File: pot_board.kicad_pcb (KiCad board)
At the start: 2 copper layers, 190.5 x 45.7 mm, 40 parts, among them J1 Power, J2 Conn 1x3, J3 Conn 1x3, J4 Conn 1x3, J5 Conn 1x3, J6 Conn 1x3, J7 Conn 1x3, J8 Conn 1x3, J9 Conn 1x3, SW1 SW_SPDT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

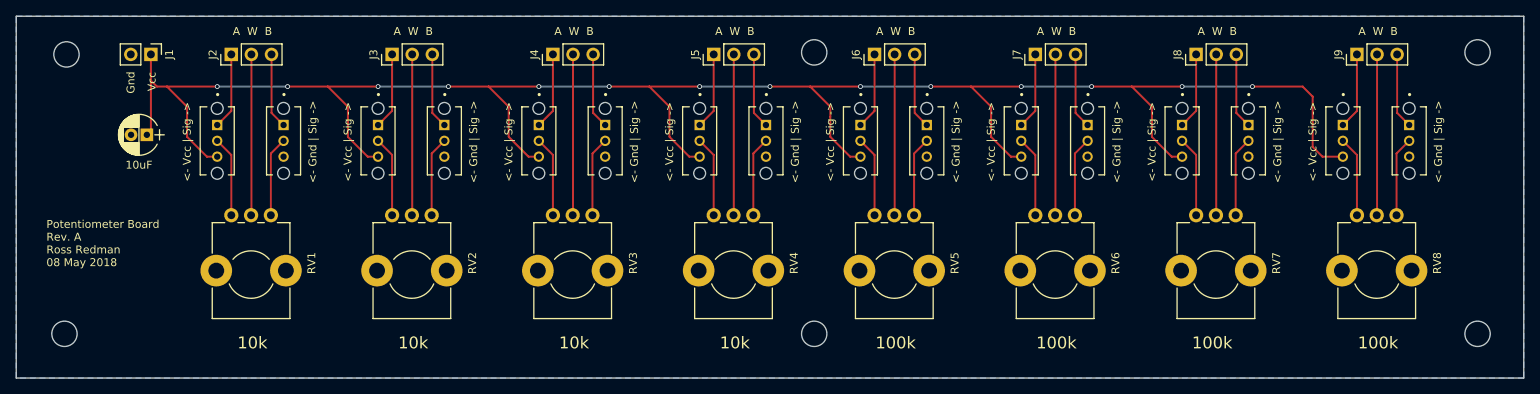
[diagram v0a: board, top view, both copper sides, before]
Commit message: Add files via upload
Re-work PCB layout with more accurate spacings for components.
Add Mecchina artwork to PCB.
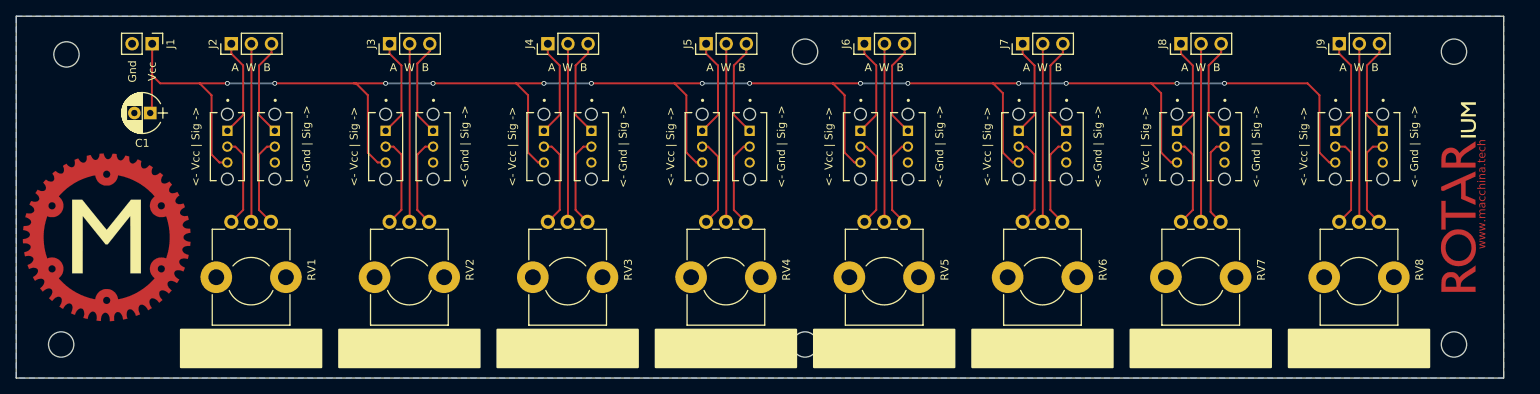
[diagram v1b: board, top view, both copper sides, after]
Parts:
- removed 10uF: CP1, Capacitors_THT:CP_Radial_D5.0mm_P2.00mm
- added C1: CP1, Capacitors_THT:CP_Radial_D5.0mm_P2.00mm, F.Cu at (37.2, 108.8)
- added G***: LOGO, Rossco Custom Library:rotarium_logo_25_6_FMask, F.Cu at (202.6, 119.4)
- added G***: LOGO, Rossco Custom Library:rotarium_logo_25_6_FCu, F.Cu at (202.6, 119.4)
- added G***: LOGO, Rossco Custom Library:ium_logo_25_6_FSilk, F.Cu at (202.6, 119.4)
- added G***: LOGO, Rossco Custom Library:macchina_logo_cogs_21mm_FCu, F.Cu at (31.8, 124.5)
- added G***: LOGO, Rossco Custom Library:macchina_logo_cogs_21mm_FMask, F.Cu at (31.8, 124.5)
- added G***: LOGO, Rossco Custom Library:macchina_logo_M_21mm, F.Cu at (31.8, 124.5)
- moved SW14 3.42 mm to (193.0, 113.0)
- moved MK4 3.27 mm to (202.0, 138.0)
- moved SW13 3.11 mm to (173.0, 113.0)
- moved MK2 2.98 mm to (202.0, 101.0)
- moved SW10 2.80 mm to (153.0, 113.0)
- moved J9 2.61 mm to (187.5, 100.0)
- moved SW9 2.49 mm to (133.0, 113.0)
- moved RV8 2.39 mm to (187.5, 122.5)
- moved J8 2.34 mm to (167.5, 100.0)
- moved SW6 2.19 mm to (113.0, 113.0)
- moved RV7 2.09 mm to (167.5, 122.5)
- moved J7 2.09 mm to (147.5, 100.0)
- moved SW5 1.89 mm to (93.0, 113.0)
- moved J6 1.86 mm to (127.5, 100.0)
- moved RV6 1.80 mm to (147.5, 122.5)
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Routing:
- net VCC: track 254.5 -> 250.6 mm
- net Net-(J9-Pad3): track 9.55 -> 12.5 mm
- net Net-(J8-Pad3): track 9.55 -> 12.5 mm
- net Net-(J7-Pad3): track 9.55 -> 12.5 mm
- net Net-(J6-Pad3): track 9.55 -> 12.5 mm
- net Net-(J2-Pad3): track 9.55 -> 12.5 mm
- net Net-(J5-Pad3): track 9.55 -> 12.5 mm
- net Net-(J4-Pad3): track 9.55 -> 12.5 mm
- net Net-(J3-Pad3): track 9.55 -> 12.5 mm
- net Net-(J9-Pad1): track 9.66 -> 12.4 mm
- net Net-(J6-Pad1): track 9.66 -> 12.4 mm
- net Net-(J5-Pad1): track 9.66 -> 12.4 mm
- net Net-(J3-Pad1): track 9.66 -> 12.4 mm
- net Net-(J2-Pad1): track 9.66 -> 12.4 mm
- net Net-(J4-Pad1): track 9.66 -> 12.4 mm
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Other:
- board size 190.5 x 45.7 mm -> 188 x 45.7 mm
- board text added: "ROTARium Rev. B Mecchina.tech 21 May 2018"
- board text added: "www.macchina.tech"
- board text added: "© Mecchina Tech 2018"
- board text removed: "100k"
- board text removed: "10k"
- board text removed: "Potentiometer Board Rev. A Ross Redman 08 May 2018"

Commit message: Add files via upload
Move switches to more ergonomic position.
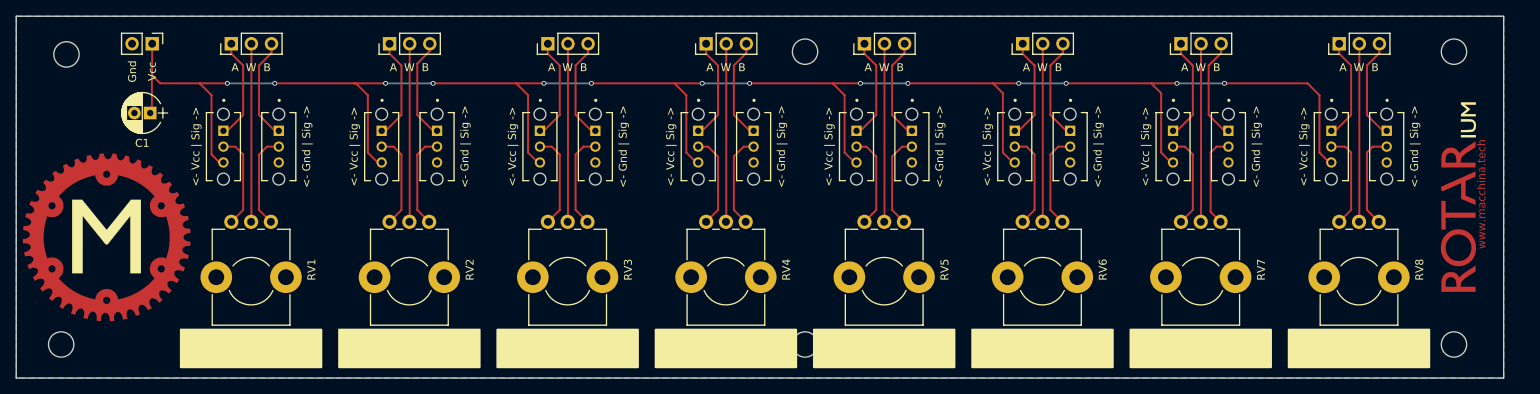
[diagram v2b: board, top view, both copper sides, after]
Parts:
- moved SW1 0.50 mm to (53.5, 113.0)
- moved SW10 0.50 mm to (153.5, 113.0)
- moved SW11 0.50 mm to (126.5, 113.0)
- moved SW12 0.50 mm to (146.5, 113.0)
- moved SW13 0.50 mm to (173.5, 113.0)
- moved SW14 0.50 mm to (193.5, 113.0)
- moved SW15 0.50 mm to (166.5, 113.0)
- moved SW16 0.50 mm to (186.5, 113.0)
- moved SW2 0.50 mm to (73.5, 113.0)
- moved SW3 0.50 mm to (46.5, 113.0)
- moved SW4 0.50 mm to (66.5, 113.0)
- moved SW5 0.50 mm to (93.5, 113.0)
- moved SW6 0.50 mm to (113.5, 113.0)
- moved SW7 0.50 mm to (86.5, 113.0)
- moved SW8 0.50 mm to (106.5, 113.0)
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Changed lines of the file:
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@@
 (kicad_pcb (version 4) (host pcbnew 4.0.7)
   (general
-    (links 0)
+    (links 58)
     (no_connects 0)
-    (area 20.269999 95.395237 208.330001 143.604762)
+    (area 20.269999 96.469999 208.330001 142.290001)
     (thickness 1.6)
     (drawings 33)
@@
     (visible_elements FFFFF77F)
     (pcbplotparams
-      (layerselection 0x010f0_80000001)
+      (layerselection 0x3ffff_80000001)
       (usegerberextensions true)
       (excludeedgelayer true)
@@
       (drillshape 0)
       (scaleselection 1)
-      (outputdirectory Pot_Board_REVA))
+      (outputdirectory Pot_Board_REVB))
   )
   (net 0 "")
@@
     (descr "Through hole straight socket strip, 1x02, 2.54mm pitch, single row")
     (tags "Through hole socket strip THT 1x02 2.54mm single row")
-    (fp_text reference J1 (at 0 -2.33 270) (layer F.SilkS)
+    (fp_text reference J1 (at 0 -2.33 270) (layer F.SilkS) hide
       (effects (font (size 1 1) (thickness 0.15)))
     )
@@
     (descr "Through hole straight socket strip, 1x03, 2.54mm pitch, single row")
     (tags "Through hole socket strip THT 1x03 2.54mm single row")
-    (fp_text reference J2 (at 0 -2.33 90) (layer F.SilkS)
+    (fp_text reference J2 (at 0 -2.33 90) (layer F.SilkS) hide
       (effects (font (size 1 1) (thickness 0.15)))
     )
@@
     (descr "Through hole straight socket strip, 1x03, 2.54mm pitch, single row")
     (tags "Through hole socket strip THT 1x03 2.54mm single row")
-    (fp_text reference J3 (at 0 -2.33 90) (layer F.SilkS)
+    (fp_text reference J3 (at 0 -2.33 90) (layer F.SilkS) hide
       (effects (font (size 1 1) (thickness 0.15)))
     )
@@
     (descr "Through hole straight socket strip, 1x03, 2.54mm pitch, single row")
     (tags "Through hole socket strip THT 1x03 2.54mm single row")
-    (fp_text reference J4 (at 0 -2.33 90) (layer F.SilkS)
+    (fp_text reference J4 (at 0 -2.33 90) (layer F.SilkS) hide
       (effects (font (size 1 1) (thickness 0.15)))
     )
@@
     (descr "Through hole straight socket strip, 1x03, 2.54mm pitch, single row")
     (tags "Through hole socket strip THT 1x03 2.54mm single row")
-    (fp_text reference J5 (at 0 -2.33 90) (layer F.SilkS)
+    (fp_text reference J5 (at 0 -2.33 90) (layer F.SilkS) hide
       (effects (font (size 1 1) (thickness 0.15)))
     )
@@
     (descr "Through hole straight socket strip, 1x03, 2.54mm pitch, single row")
     (tags "Through hole socket strip THT 1x03 2.54mm single row")
-    (fp_text reference J6 (at 0 -2.33 90) (layer F.SilkS)
+    (fp_text reference J6 (at 0 -2.33 90) (layer F.SilkS) hide
       (effects (font (size 1 1) (thickness 0.15)))
     )
@@
     (descr "Through hole straight socket strip, 1x03, 2.54mm pitch, single row")
     (tags "Through hole socket strip THT 1x03 2.54mm single row")
-    (fp_text reference J7 (at 0 -2.33 90) (layer F.SilkS)
+    (fp_text reference J7 (at 0 -2.33 90) (layer F.SilkS) hide
       (effects (font (size 1 1) (thickness 0.15)))
     )
@@
     (descr "Through hole straight socket strip, 1x03, 2.54mm pitch, single row")
     (tags "Through hole socket strip THT 1x03 2.54mm single row")
-    (fp_text reference J8 (at 0 -2.33 90) (layer F.SilkS)
+    (fp_text reference J8 (at 0 -2.33 90) (layer F.SilkS) hide
       (effects (font (size 1 1) (thickness 0.15)))
     )
@@
     (descr "Through hole straight socket strip, 1x03, 2.54mm pitch, single row")
     (tags "Through hole socket strip THT 1x03 2.54mm single row")
-    (fp_text reference J9 (at 0 -2.33 90) (layer F.SilkS)
+    (fp_text reference J9 (at 0 -2.33 90) (layer F.SilkS) hide
       (effects (font (size 1 1) (thickness 0.15)))
     )
@@
   )
   (module OS102011MS2QN1:SW_OS102011MS2QN1 (layer F.Cu)
-    (at 53 113 270)
+    (at 53.5 113 270)
     (fp_text reference SW1 (at -3.28175 -3.30576 270) (layer F.SilkS) hide
       (effects (font (size 0.48014 0.48014) (thickness 0.05)))
@@
   )
   (module OS102011MS2QN1:SW_OS102011MS2QN1 (layer F.Cu)
-    (at 47 113 270)
+    (at 46.5 113 270)
     (fp_text reference SW3 (at -3.28175 -3.30576 270) (layer F.SilkS) hide
       (effects (font (size 0.48014 0.48014) (thickness 0.05)))
@@
   )
   (module OS102011MS2QN1:SW_OS102011MS2QN1 (layer F.Cu)
-    (at 67 113 270)
+    (at 66.5 113 270)
     (fp_text reference SW4 (at -3.28175 -3.30576 270) (layer F.SilkS) hide
       (effects (font (size 0.48014 0.48014) (thickness 0.05)))
@@
   )
   (module OS102011MS2QN1:SW_OS102011MS2QN1 (layer F.Cu)
-    (at 93 113 270)
+    (at 93.5 113 270)
     (fp_text reference SW5 (at -3.28175 -3.30576 270) (layer F.SilkS) hide
       (effects (font (size 0.48014 0.48014) (thickness 0.05)))
@@
   )
   (module OS102011MS2QN1:SW_OS102011MS2QN1 (layer F.Cu)
-    (at 113 113 270)
+    (at 113.5 113 270)
     (fp_text reference SW6 (at -3.28175 -3.30576 270) (layer F.SilkS) hide
       (effects (font (size 0.48014 0.48014) (thickness 0.05)))
@@
   )
   (module OS102011MS2QN1:SW_OS102011MS2QN1 (layer F.Cu)
-    (at 87 113 270)
+    (at 86.5 113 270)
     (fp_text reference SW7 (at -3.28175 -3.30576 270) (layer F.SilkS) hide
       (effects (font (size 0.48014 0.48014) (thickness 0.05)))
@@
   )
   (module OS102011MS2QN1:SW_OS102011MS2QN1 (layer F.Cu)
-    (at 107 113 270)
+    (at 106.5 113 270)
     (fp_text reference SW8 (at -3.28175 -3.30576 270) (layer F.SilkS) hide
       (effects (font (size 0.48014 0.48014) (thickness 0.05)))
@@
   )
   (module OS102011MS2QN1:SW_OS102011MS2QN1 (layer F.Cu)
-    (at 133 113 270)
+    (at 133.5 113 270)
     (fp_text reference SW9 (at -3.28175 -3.30576 270) (layer F.SilkS) hide
       (effects (font (size 0.48014 0.48014) (thickness 0.05)))
@@
   )
   (module OS102011MS2QN1:SW_OS102011MS2QN1 (layer F.Cu)
-    (at 153 113 270)
+    (at 153.5 113 270)
     (fp_text reference SW10 (at -3.28175 -3.30576 270) (layer F.SilkS) hide
       (effects (font (size 0.48014 0.48014) (thickness 0.05)))
@@
   )
   (module OS102011MS2QN1:SW_OS102011MS2QN1 (layer F.Cu)
-    (at 127 113 270)
+    (at 126.5 113 270)
     (fp_text reference SW11 (at -3.28175 -3.30576 270) (layer F.SilkS) hide
       (effects (font (size 0.48014 0.48014) (thickness 0.05)))
@@
   )
   (module OS102011MS2QN1:SW_OS102011MS2QN1 (layer F.Cu)
-    (at 147 113 270)
+    (at 146.5 113 270)
     (fp_text reference SW12 (at -3.28175 -3.30576 270) (layer F.SilkS) hide
       (effects (font (size 0.48014 0.48014) (thickness 0.05)))
@@
   )
   (module OS102011MS2QN1:SW_OS102011MS2QN1 (layer F.Cu)
-    (at 173 113 270)
+    (at 173.5 113 270)
     (fp_text reference SW13 (at -3.28175 -3.30576 270) (layer F.SilkS) hide
       (effects (font (size 0.48014 0.48014) (thickness 0.05)))
@@
   )
   (module OS102011MS2QN1:SW_OS102011MS2QN1 (layer F.Cu)
-    (at 193 113 270)
+    (at 193.5 113 270)
     (fp_text reference SW14 (at -3.28175 -3.30576 270) (layer F.SilkS) hide
       (effects (font (size 0.48014 0.48014) (thickness 0.05)))
@@
   )
   (module OS102011MS2QN1:SW_OS102011MS2QN1 (layer F.Cu)
-    (at 167 113 270)
+    (at 166.5 113 270)
     (fp_text reference SW15 (at -3.28175 -3.30576 270) (layer F.SilkS) hide
       (effects (font (size 0.48014 0.48014) (thickness 0.05)))
@@
   )
   (module OS102011MS2QN1:SW_OS102011MS2QN1 (layer F.Cu)
-    (at 187 113 270)
+    (at 186.5 113 270)
     (fp_text reference SW16 (at -3.28175 -3.30576 270) (layer F.SilkS) hide
       (effects (font (size 0.48014 0.48014) (thickness 0.05)))
@@
   )
   (module OS102011MS2QN1:SW_OS102011MS2QN1 (layer F.Cu)
-    (at 73 113 270)
+    (at 73.5 113 270)
     (fp_text reference SW2 (at -3.28345 -3.30747 270) (layer F.SilkS) hide
       (effects (font (size 0.480388 0.480388) (thickness 0.05)))
